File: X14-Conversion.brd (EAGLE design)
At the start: 160 x 100 mm, 23 parts, among them P1 282837-2, P2 282837-2, P3 282837-2, U2 LM2678SD-ADJ/NOPB

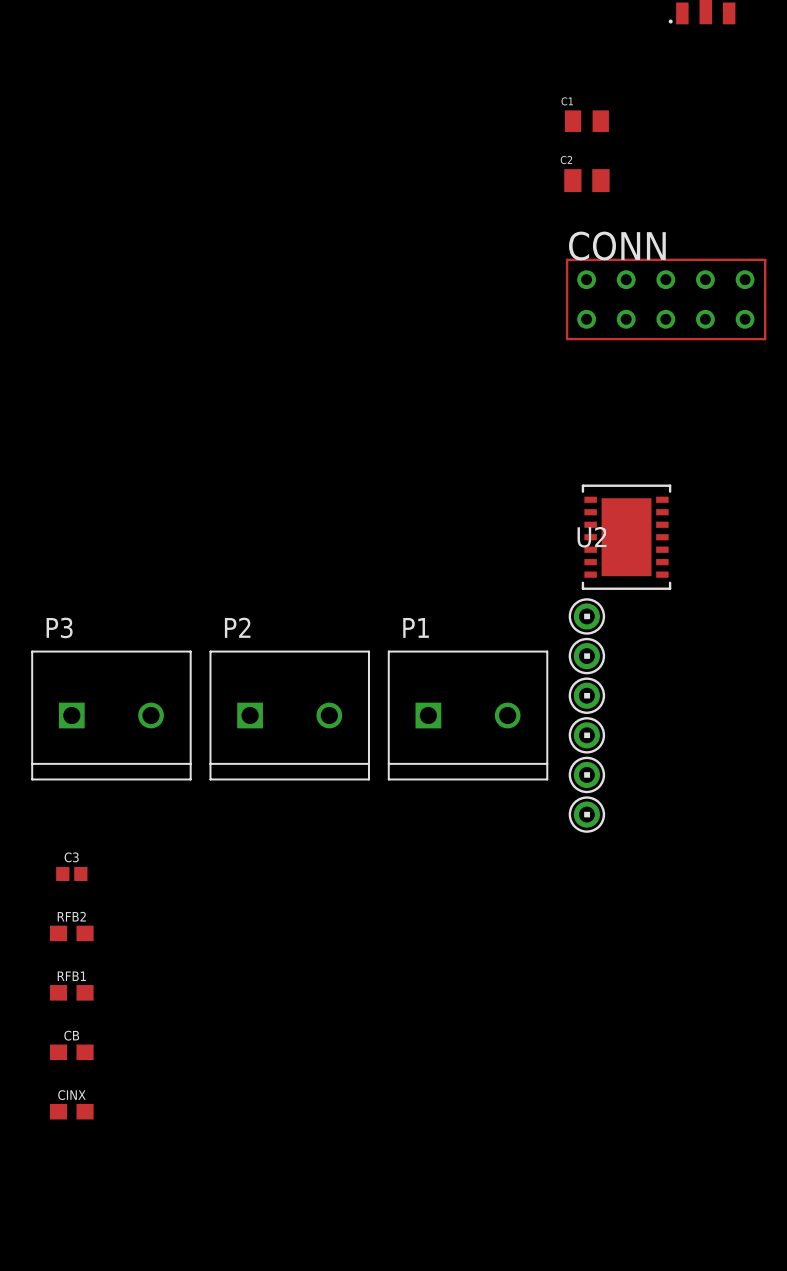
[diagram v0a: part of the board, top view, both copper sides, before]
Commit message: Fix capacitors on Linear Regulator
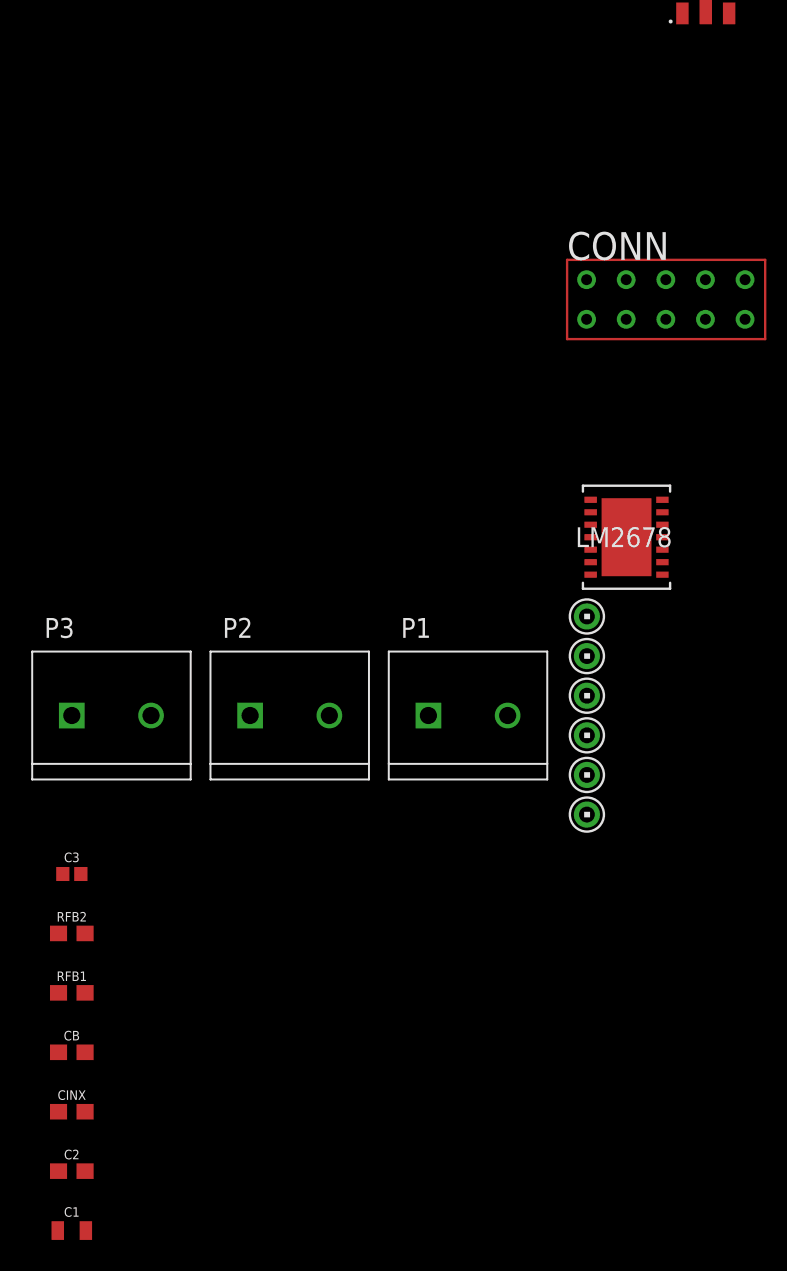
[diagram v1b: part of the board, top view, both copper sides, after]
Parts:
- AZ1117C: value SOT150P410X160-3N -> AZ1117C-3.3
- C1: value 10uF 16V -> 22uF; device CAP_GRM21BR61C106KE15L:CAPC2012X135N -> SparkFun-Capacitors:0805
- C2: value 22uF 16V -> 10uF; device CAP_GRM21BR61C226ME44L:CAPC2012X145N -> SparkFun-Capacitors:0603
- moved C1 78.4 mm to (-92.7, -48.3)
- moved C2 71.6 mm to (-92.7, -44.5)
- renumbered U$1 to AZ1117C, U2 to LM2678
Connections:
- net 3.3V: now also C2.1; no longer C1.1
- net 5.2V: now also C1.1; no longer C2.1
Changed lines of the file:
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@@
 <attribute name="VALUE" x="-46.18" y="45.816" size="1.27" layer="27" align="top-left"/>
 </element>
-<element name="U$1" library="AZ1117C-3.3" package="SOT150P410X160-3N" value="SOT150P410X160-3N" x="-52.07" y="31.75" smashed="yes">
+<element name="AZ1117C" library="AZ1117C-3.3" package="SOT150P410X160-3N" value="AZ1117C-3.3" x="-52.07" y="31.75" smashed="yes">
 <attribute name="NAME" x="-59.741959375" y="35.952740625" size="3.2051" layer="25" display="off"/>
 <attribute name="VALUE" x="-60.214790625" y="26.2387" size="1.27" layer="27"/>
 </element>
-<element name="C1" library="CAP_GRM21BR61C106KE15L" package="CAPC2012X135N" value="10uF 16V" x="-59.69" y="22.86" smashed="yes">
-<attribute name="DESCRIPTION" value=" 10 µF ±10% 16V Ceramic Capacitor X5R 0805 (2012 Metric) " x="-59.69" y="22.86" size="1.778" layer="27" display="off"/>
-<attribute name="DIGI-KEY_PART_NUMBER" value="490-3886-2-ND" x="-59.69" y="22.86" size="1.778" layer="27" display="off"/>
-<attribute name="MF" value="Murata" x="-59.69" y="22.86" size="1.778" layer="27" display="off"/>
-<attribute name="MP" value="GRM21BR61C106KE15L" x="-59.69" y="22.86" size="1.778" layer="27" display="off"/>
-<attribute name="NAME" x="-61.35" y="23.88" size="0.5" layer="25"/>
-<attribute name="PACKAGE" value="2012 Murata" x="-59.69" y="22.86" size="1.778" layer="27" display="off"/>
-<attribute name="PURCHASE-URL" value="https://pricing.snapeda.com/search/part/GRM21BR61C106KE15L/?ref=eda" x="-59.69" y="22.86" size="1.778" layer="27" display="off"/>
-<attribute name="VALUE" x="-61.35" y="21.84" size="0.5" layer="27" align="top-left"/>
-</element>
-<element name="C2" library="CAP_GRM21BR61C226ME44L" package="CAPC2012X145N" value="22uF 16V" x="-59.69" y="19.05" smashed="yes">
-<attribute name="DESCRIPTION" value=" SMD Capacitor X5R(EIA) with Capacitance: 22uF Tol. 20%. Rated Voltage: 16Vdc " x="-59.69" y="19.05" size="1.778" layer="27" display="off"/>
-<attribute name="DIGI-KEY_PART_NUMBER" value="490-10747-2-ND" x="-59.69" y="19.05" size="1.778" layer="27" display="off"/>
-<attribute name="MF" value="Murata" x="-59.69" y="19.05" size="1.778" layer="27" display="off"/>
-<attribute name="MP" value="GRM21BR61C226ME44L" x="-59.69" y="19.05" size="1.778" layer="27" display="off"/>
-<attribute name="NAME" x="-61.4" y="20.12" size="0.5" layer="25"/>
-<attribute name="PACKAGE" value="2012 Murata" x="-59.69" y="19.05" size="1.778" layer="27" display="off"/>
-<attribute name="PURCHASE-URL" value="https://pricing.snapeda.com/search/part/GRM21BR61C226ME44L/?ref=eda" x="-59.69" y="19.05" size="1.778" layer="27" display="off"/>
-<attribute name="VALUE" x="-61.4" y="17.98" size="0.5" layer="27" align="top-left"/>
-</element>
 <element name="CONN" library="CONN, Distribution-Conversion" package="TSW-105-05-G-S" value="DISTRIBUTION-CONVERSION" x="-54.61" y="12.7" smashed="yes">
 <attribute name="NAME" x="-60.96" y="13.97" size="1.778" layer="25"/>
 </element>
-<element name="U2" library="LM2678SX-ADJNOPB" package="SRC14A" value="LM2678SD-ADJ/NOPB" x="-57.15" y="-3.81" smashed="yes">
+<element name="LM2678" library="LM2678SX-ADJNOPB" package="SRC14A" value="LM2678SD-ADJ/NOPB" x="-57.15" y="-3.81" smashed="yes">
 <attribute name="COPYRIGHT" value="Copyright (C) 2021 Ultra Librarian. All rights reserved." x="-57.15" y="-3.81" size="1.778" layer="27" display="off"/>
 <attribute name="DIGI-KEY_PART_NUMBER_1" value="2156-LM2678SD-ADJ/NOPB-ND" x="-57.15" y="-3.81" size="1.778" layer="27" display="off"/>
@@
 <attribute name="VALUE" x="-92.71" y="-41.402" size="0.6096" layer="27" font="vector" ratio="20" align="top-center"/>
 </element>
+<element name="C2" library="SparkFun-Capacitors" library_urn="urn:adsk.eagle:library:510" package="0603" package3d_urn="urn:adsk.eagle:package:37414/1" value="10uF" x="-92.71" y="-44.45" smashed="yes">
+<attribute name="NAME" x="-92.71" y="-43.688" size="0.6096" layer="25" font="vector" ratio="20" align="bottom-center"/>
+<attribute name="PROD_ID" value="CAP-11015" x="-92.71" y="-44.45" size="1.778" layer="27" display="off"/>
+<attribute name="VALUE" x="-92.71" y="-45.212" size="0.6096" layer="27" font="vector" ratio="20" align="top-center"/>
+</element>
+<element name="C1" library="SparkFun-Capacitors" library_urn="urn:adsk.eagle:library:510" package="0805" package3d_urn="urn:adsk.eagle:package:37429/1" value="22uF" x="-92.71" y="-48.26" smashed="yes">
+<attribute name="NAME" x="-92.71" y="-47.371" size="0.6096" layer="25" font="vector" ratio="20" align="bottom-center"/>
+<attribute name="PROD_ID" value="CAP-08402" x="-92.71" y="-48.26" size="1.778" layer="27" display="off"/>
+<attribute name="VALUE" x="-92.71" y="-49.149" size="0.6096" layer="27" font="vector" ratio="20" align="top-center"/>
+</element>
 </elements>
 <signals>
 <signal name="GND">
-<contactref element="C2" pad="2"/>
-<contactref element="U$1" pad="1"/>
-<contactref element="C1" pad="2"/>
+<contactref element="AZ1117C" pad="1"/>
 <contactref element="CONN" pad="5"/>
 <contactref element="CONN" pad="4"/>
 <contactref element="D1" pad="2"/>
 <contactref element="COUT" pad="2"/>
-<contactref element="U2" pad="9"/>
-<contactref element="U2" pad="15"/>
+<contactref element="LM2678" pad="9"/>
+<contactref element="LM2678" pad="15"/>
 <contactref element="CIN" pad="2"/>
 <contactref element="U$5" pad="GND"/>
@@
 <contactref element="RFB1" pad="2"/>
 <contactref element="CINX" pad="2"/>
+<contactref element="C1" pad="2"/>
+<contactref element="C2" pad="2"/>
+<wire x1="-91.86" y1="-44.45" x2="-91.81" y2="-48.26" width="0" layer="19" extent="1-1"/>
+<wire x1="-91.86" y1="-40.64" x2="-91.86" y2="-44.45" width="0" layer="19" extent="1-1"/>
 <wire x1="-91.86" y1="-33.02" x2="-91.86" y2="-40.64" width="0" layer="19" extent="1-1"/>
 <wire x1="-92.13" y1="-25.4" x2="-91.86" y2="-33.02" width="0" layer="19" extent="1-1"/>
@@
 <wire x1="-49.55" y1="10.16" x2="-52.09" y2="10.16" width="0" layer="19" extent="1-1"/>
 <wire x1="-49.55" y1="12.7" x2="-52.09" y2="12.7" width="0" layer="19" extent="1-1"/>
-<wire x1="-58.79" y1="19.05" x2="-52.09" y2="12.7" width="0" layer="19" extent="1-1"/>
-<wire x1="-58.802" y1="22.86" x2="-58.79" y2="19.05" width="0" layer="19" extent="1-1"/>
-<wire x1="-53.569" y1="29.769" x2="-58.802" y2="22.86" width="0" layer="19" extent="1-1"/>
+<wire x1="-53.569" y1="29.769" x2="-52.09" y2="12.7" width="0" layer="19" extent="1-1"/>
 <wire x1="-38.83" y1="52.07" x2="-53.569" y2="29.769" width="0" layer="19" extent="1-1"/>
 <wire x1="-26.4541" y1="67.31" x2="-38.83" y2="52.07" width="0" layer="19" extent="1-1"/>
@@
 </signal>
 <signal name="3.3V">
-<contactref element="U$1" pad="2"/>
-<contactref element="C1" pad="1"/>
+<contactref element="AZ1117C" pad="2"/>
 <contactref element="CONN" pad="2"/>
 <contactref element="U$2" pad="3.3V"/>
 <contactref element="P1" pad="2"/>
 <contactref element="CONN" pad="7"/>
+<contactref element="C2" pad="1"/>
+<wire x1="-64.77" y1="-15.24" x2="-93.56" y2="-44.45" width="0" layer="19" extent="1-1"/>
 <wire x1="-59.69" y1="-8.89" x2="-64.77" y2="-15.24" width="0" layer="19" extent="1-1"/>
 <wire x1="-57.17" y1="10.16" x2="-59.69" y2="-8.89" width="0" layer="19" extent="1-1"/>
 <wire x1="-57.17" y1="12.7" x2="-57.17" y2="10.16" width="0" layer="19" extent="1-1"/>
-<wire x1="-60.578" y1="22.86" x2="-57.17" y2="12.7" width="0" layer="19" extent="1-1"/>
-<wire x1="-52.07" y1="30.023" x2="-60.578" y2="22.86" width="0" layer="19" extent="1-1"/>
+<wire x1="-52.07" y1="30.023" x2="-57.17" y2="12.7" width="0" layer="19" extent="1-1"/>
 </signal>
 <signal name="5.2V">
-<contactref element="U$1" pad="3"/>
-<contactref element="C2" pad="1"/>
+<contactref element="AZ1117C" pad="3"/>
 <contactref element="CONN" pad="3"/>
 <contactref element="L1" pad="2"/>
@@
 <contactref element="C3" pad="1"/>
 <contactref element="RFB2" pad="2"/>
+<contactref element="C1" pad="1"/>
+<wire x1="-91.86" y1="-29.21" x2="-93.61" y2="-48.26" width="0" layer="19" extent="1-1"/>
 <wire x1="-93.29" y1="-25.4" x2="-91.86" y2="-29.21" width="0" layer="19" extent="1-1"/>
 <wire x1="-69.85" y1="-15.24" x2="-93.29" y2="-25.4" width="0" layer="19" extent="1-1"/>
@@
 <wire x1="-54.63" y1="10.16" x2="-59.69" y2="-11.43" width="0" layer="19" extent="1-1"/>
 <wire x1="-54.63" y1="12.7" x2="-54.63" y2="10.16" width="0" layer="19" extent="1-1"/>
-<wire x1="-60.59" y1="19.05" x2="-54.63" y2="12.7" width="0" layer="19" extent="1-1"/>
-<wire x1="-50.571" y1="29.769" x2="-60.59" y2="19.05" width="0" layer="19" extent="1-1"/>
+<wire x1="-50.571" y1="29.769" x2="-54.63" y2="12.7" width="0" layer="19" extent="1-1"/>
 <wire x1="-47.53" y1="52.07" x2="-50.571" y2="29.769" width="0" layer="19" extent="1-1"/>
 <wire x1="-21.07" y1="53.34" x2="-47.53" y2="52.07" width="0" layer="19" extent="1-1"/>
@@
 <signal name="12V">
 <contactref element="CONN" pad="1"/>
-<contactref element="U2" pad="3"/>
+<contactref element="LM2678" pad="3"/>
 <contactref element="CIN" pad="1"/>
 <contactref element="U$4" pad="12V"/>
@@
 </signal>
 <signal name="N$2">
-<contactref element="U2" pad="14"/>
+<contactref element="LM2678" pad="14"/>
 <contactref element="L1" pad="1"/>
 <contactref element="D1" pad="1"/>
@@
 </signal>
 <signal name="N$4">
-<contactref element="U2" pad="4"/>
+<contactref element="LM2678" pad="4"/>
 <contactref element="CB" pad="1"/>
 <wire x1="-59.45" y1="-3.81" x2="-93.56" y2="-36.83" width="0" layer="19" extent="1-1"/>
 </signal>
 <signal name="N$5">
-<contactref element="U2" pad="7"/>
+<contactref element="LM2678" pad="7"/>
 <contactref element="RFB1" pad="1"/>
 <contactref element="RFB2" pad="1"/>

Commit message: Fix Footprints
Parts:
- D1: device CDBC520-G_Library:CDBC-G -> CDBC520-G_Library:CDBG520-G
- moved D1 153.5 mm to (-102.9, -59.7)
- moved CIN 141.1 mm to (-85.1, -62.2)
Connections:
- net 3.3V: now also AZ1117C.4
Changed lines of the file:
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@@
 </autorouter>
 <elements>
-<element name="D1" library="CDBC520-G_Library" package="CDBC-G" value="550mV 5A" x="-29.21" y="74.93" smashed="yes">
-<attribute name="COPYRIGHT" value="Copyright (C) 2021 Ultra Librarian. All rights reserved." x="-29.21" y="74.93" size="1.778" layer="27" display="off"/>
-<attribute name="DIGI-KEY_PART_NUMBER_1" value="641-1125-1-ND" x="-29.21" y="74.93" size="1.778" layer="27" display="off"/>
-<attribute name="DIGI-KEY_PART_NUMBER_2" value="641-1125-2-ND" x="-29.21" y="74.93" size="1.778" layer="27" display="off"/>
-<attribute name="DIGI-KEY_PART_NUMBER_3" value="641-1125-6-ND" x="-29.21" y="74.93" size="1.778" layer="27" display="off"/>
-<attribute name="MANUFACTURER_PART_NUMBER" value="CDBC520-G" x="-29.21" y="74.93" size="1.778" layer="27" display="off"/>
-<attribute name="MFR_NAME" value="Comchip" x="-29.21" y="74.93" size="1.778" layer="27" display="off"/>
-<attribute name="NAME" x="-32.4812" y="74.295" size="1.27" layer="25" ratio="6"/>
-<attribute name="VALUE" x="-30.9388" y="74.295" size="1.27" layer="27" ratio="6"/>
-</element>
-<element name="CIN" library="20SVPF120M" package="PCAP_SVP_C6_PAN" value="120uF 25mΩ" x="-29.21" y="67.31" smashed="yes">
-<attribute name="COPYRIGHT" value="Copyright (C) 2021 Ultra Librarian. All rights reserved." x="-29.21" y="67.31" size="1.778" layer="27" display="off"/>
-<attribute name="DIGI-KEY_PART_NUMBER_1" value="P16498CT-ND" x="-29.21" y="67.31" size="1.778" layer="27" display="off"/>
-<attribute name="DIGI-KEY_PART_NUMBER_2" value="P16498DKR-ND" x="-29.21" y="67.31" size="1.778" layer="27" display="off"/>
-<attribute name="DIGI-KEY_PART_NUMBER_3" value="P16498TR-ND" x="-29.21" y="67.31" size="1.778" layer="27" display="off"/>
-<attribute name="MANUFACTURER_PART_NUMBER" value="20SVPF120M" x="-29.21" y="67.31" size="1.778" layer="27" display="off"/>
-<attribute name="MFR_NAME" value="Panasonic" x="-29.21" y="67.31" size="1.778" layer="27" display="off"/>
-<attribute name="NAME" x="-32.4812" y="66.675" size="1.27" layer="25" ratio="6"/>
-<attribute name="VALUE" x="-30.9388" y="66.675" size="1.27" layer="27" ratio="6"/>
-</element>
 <element name="L1" library="IND, 15uH - hcma1305" package="HCMA1305" package3d_urn="urn:adsk.eagle:package:24201702/2" value="15uH" x="-26.67" y="53.34" smashed="yes">
 <attribute name="NAME" x="-26.67" y="57.15" size="1.27" layer="25" align="bottom-center"/>
@@
 <attribute name="VALUE" x="-92.71" y="-49.149" size="0.6096" layer="27" font="vector" ratio="20" align="top-center"/>
 </element>
+<element name="D1" library="CDBC520-G_Library" package="CDBG520-G" value="550mV 5A" x="-102.87" y="-59.69" smashed="yes"/>
+<element name="CIN" library="20SVPF120M" package="PCAP_SVP_C6_PAN" value="120uF 25mΩ" x="-85.09" y="-62.23" smashed="yes"/>
 </elements>
 <signals>
@@
 <contactref element="CONN" pad="5"/>
 <contactref element="CONN" pad="4"/>
-<contactref element="D1" pad="2"/>
 <contactref element="COUT" pad="2"/>
 <contactref element="LM2678" pad="9"/>
 <contactref element="LM2678" pad="15"/>
-<contactref element="CIN" pad="2"/>
 <contactref element="U$5" pad="GND"/>
 <contactref element="U$6" pad="GND"/>
@@
 <contactref element="C1" pad="2"/>
 <contactref element="C2" pad="2"/>
+<contactref element="D1" pad="2"/>
+<contactref element="CIN" pad="2"/>
+<wire x1="-82.3341" y1="-62.23" x2="-95.87" y2="-62.8" width="0" layer="19" extent="1-1"/>
+<wire x1="-91.81" y1="-48.26" x2="-95.87" y2="-62.8" width="0" layer="19" extent="1-1"/>
 <wire x1="-91.86" y1="-44.45" x2="-91.81" y2="-48.26" width="0" layer="19" extent="1-1"/>
 <wire x1="-91.86" y1="-40.64" x2="-91.86" y2="-44.45" width="0" layer="19" extent="1-1"/>
@@
 <wire x1="-53.569" y1="29.769" x2="-52.09" y2="12.7" width="0" layer="19" extent="1-1"/>
 <wire x1="-38.83" y1="52.07" x2="-53.569" y2="29.769" width="0" layer="19" extent="1-1"/>
-<wire x1="-26.4541" y1="67.31" x2="-38.83" y2="52.07" width="0" layer="19" extent="1-1"/>
-<wire x1="-26.083" y1="74.93" x2="-26.4541" y2="67.31" width="0" layer="19" extent="1-1"/>
 </signal>
 <signal name="3.3V">
@@
 <contactref element="CONN" pad="7"/>
 <contactref element="C2" pad="1"/>
+<contactref element="AZ1117C" pad="4"/>
 <wire x1="-64.77" y1="-15.24" x2="-93.56" y2="-44.45" width="0" layer="19" extent="1-1"/>
 <wire x1="-59.69" y1="-8.89" x2="-64.77" y2="-15.24" width="0" layer="19" extent="1-1"/>
 <wire x1="-57.17" y1="10.16" x2="-59.69" y2="-8.89" width="0" layer="19" extent="1-1"/>
 <wire x1="-57.17" y1="12.7" x2="-57.17" y2="10.16" width="0" layer="19" extent="1-1"/>
-<wire x1="-52.07" y1="30.023" x2="-57.17" y2="12.7" width="0" layer="19" extent="1-1"/>
+<wire x1="-52.07" y1="29.869" x2="-57.17" y2="12.7" width="0" layer="19" extent="1-1"/>
+<wire x1="-52.07" y1="32.639" x2="-52.07" y2="29.869" width="0" layer="19" extent="1-1"/>
 </signal>
 <signal name="5.2V">
@@
 <contactref element="CONN" pad="1"/>
 <contactref element="LM2678" pad="3"/>
-<contactref element="CIN" pad="1"/>
 <contactref element="U$4" pad="12V"/>
 <contactref element="P2" pad="2"/>
 <contactref element="CONN" pad="6"/>
 <contactref element="CINX" pad="1"/>
+<contactref element="CIN" pad="1"/>
+<wire x1="-93.56" y1="-40.64" x2="-87.8459" y2="-62.23" width="0" layer="19" extent="1-1"/>
 <wire x1="-76.2" y1="-15.24" x2="-93.56" y2="-40.64" width="0" layer="19" extent="1-1"/>
 <wire x1="-59.69" y1="-13.97" x2="-76.2" y2="-15.24" width="0" layer="19" extent="1-1"/>
@@
 <wire x1="-59.71" y1="10.16" x2="-59.45" y2="-3.01" width="0" layer="19" extent="1-1"/>
 <wire x1="-59.71" y1="12.7" x2="-59.71" y2="10.16" width="0" layer="19" extent="1-1"/>
-<wire x1="-31.9659" y1="67.31" x2="-59.71" y2="12.7" width="0" layer="19" extent="1-1"/>
 </signal>
 <signal name="N$2">
 <contactref element="LM2678" pad="14"/>
 <contactref element="L1" pad="1"/>
+<contactref element="CB" pad="2"/>
 <contactref element="D1" pad="1"/>
-<contactref element="CB" pad="2"/>
+<wire x1="-91.86" y1="-36.83" x2="-102.77" y2="-62.8" width="0" layer="19" extent="1-1"/>
 <wire x1="-54.85" y1="-1.41" x2="-91.86" y2="-36.83" width="0" layer="19" extent="1-1"/>
 <wire x1="-32.27" y1="53.34" x2="-54.85" y2="-1.41" width="0" layer="19" extent="1-1"/>
-<wire x1="-32.337" y1="74.93" x2="-32.27" y2="53.34" width="0" layer="19" extent="1-1"/>
 </signal>
 <signal name="N$4">

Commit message: Fix footprints and update dimension
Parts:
- moved CIN 160.0 mm to (33.0, 45.7)
- moved D1 159.2 mm to (29.2, 29.2)
- moved C2 152.2 mm to (44.5, 21.6)
- moved C3 152.2 mm to (44.5, 40.6)
- moved CB 152.2 mm to (44.5, 29.2)
- moved CINX 152.2 mm to (44.5, 25.4)
- moved RFB1 152.2 mm to (44.5, 33.0)
- moved RFB2 152.2 mm to (44.5, 36.8)
- moved C1 151.7 mm to (44.2, 17.0)
- moved P2 125.3 mm to (44.5, 7.62)
- moved P3 109.1 mm to (16.5, 7.62)
- moved P1 101.7 mm to (31.8, 7.62)
- moved LM2678 74.7 mm to (14.0, 19.1)
- moved CONN 72.3 mm to (14.0, 35.6)
- moved U$2 70.8 mm to (6.35, 16.5)
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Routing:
- net 12V: track 0.00 -> 1.05 mm
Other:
- board size 160 x 100 mm -> 50.8 x 76.2 mm
